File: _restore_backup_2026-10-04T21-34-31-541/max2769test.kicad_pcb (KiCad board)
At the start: 4 copper layers, 166 parts, among them J1 Conn_Coaxial, J2 RJ45_JK0654219, J3 Conn_01x03_Socket, J4 Conn_01x05_Pin, J5 USB_C_Receptacle_PowerOnly_6P, SW1 SW_Push, U1 MAX2769B, U10 TPS22918, U11 TPS22918, U12 BY25Q16AW, U2 ICE40UP5K-SG48ITR, U3 STM32C051K6T6, U4 TPS7A20, U5 TPS7A20, U6 TX22-M010S, U7 TPS7A20, U8 RTL8211FD, U9 TPS7A20, Y1 TSX-3225

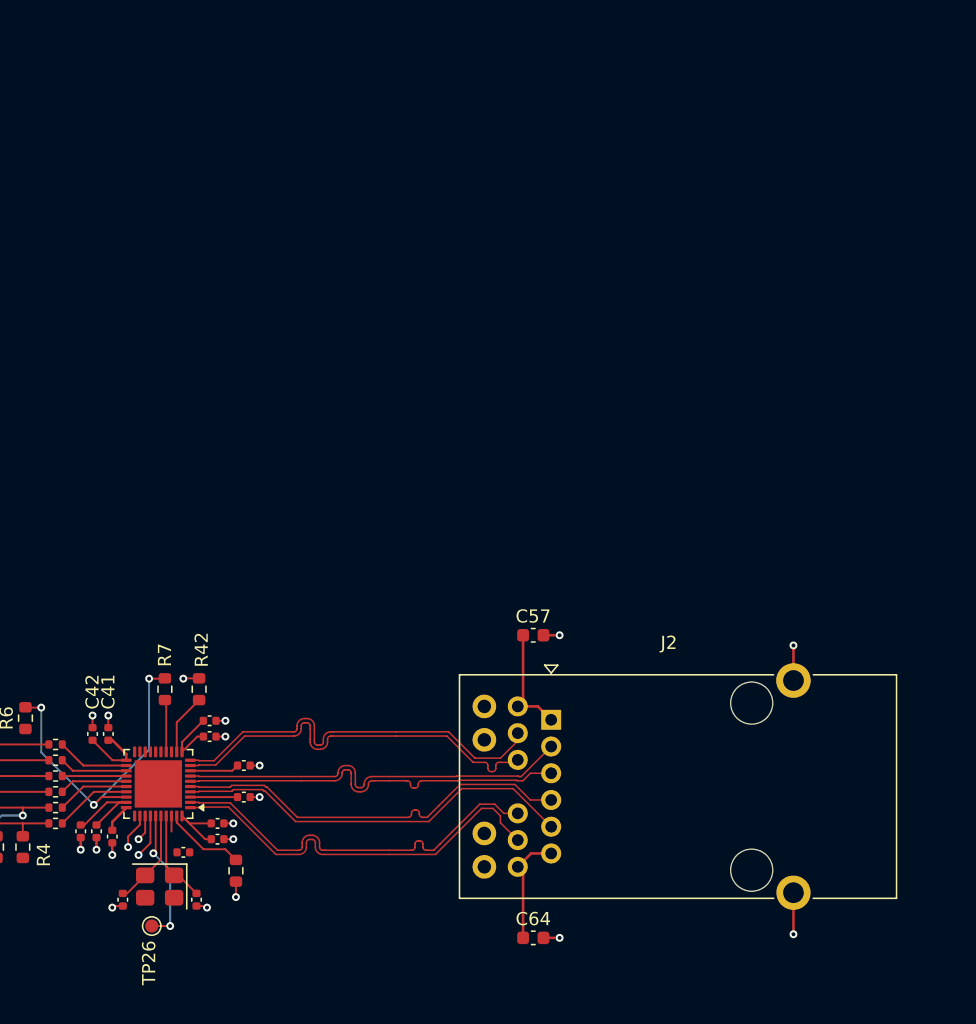
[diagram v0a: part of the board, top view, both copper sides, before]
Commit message: work on PHY layout
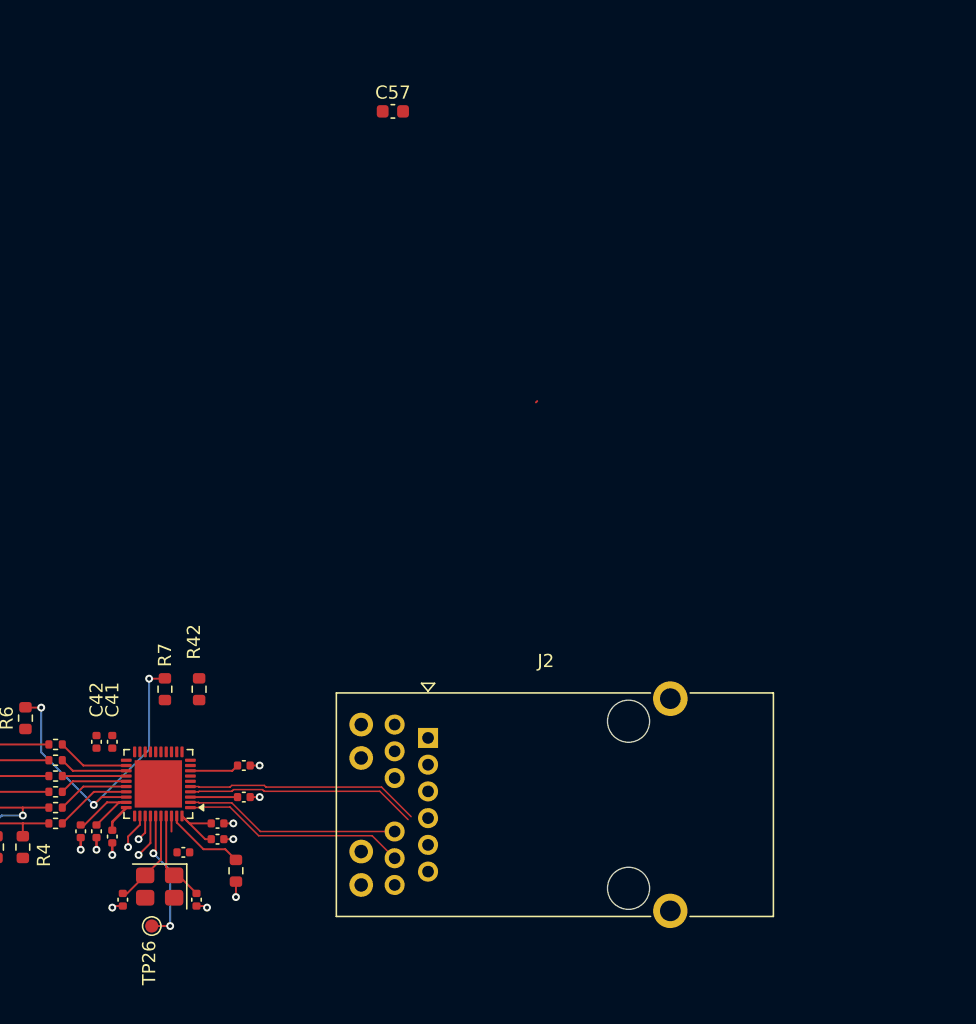
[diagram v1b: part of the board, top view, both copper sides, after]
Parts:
- removed C64: 100p, Capacitor_SMD:C_0603_1608Metric
- removed C65: 4.7u, Capacitor_SMD:C_0402_1005Metric
- removed C66: 100n, Capacitor_SMD:C_0402_1005Metric
- moved C57 41.2 mm to (194.3, 45.7)
- moved J2 9.46 mm to (197.0, 93.3)
- moved C41 0.67 mm to (173.0, 93.6)
- moved C42 0.67 mm to (171.8, 93.6)
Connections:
- C57 pad 1: Net-(J2-MXCT3) -> Net-(J2-MXCT1)
- J2 pad 1: Net-(J2-MXCT3) -> Net-(J2-MXCT1)
- J2 pad 4: /PHY_BI_DB_N -> /PHY_BI_DB_P
- J2 pad 5: /PHY_BI_DB_P -> /PHY_BI_DB_N
- J2 pad 7: Net-(J2-MXCT3) -> Net-(J2-MXCT1)
- J2 pad 8: /PHY_BI_DD_N -> /PHY_BI_DD_P
- J2 pad 9: /PHY_BI_DD_P -> /PHY_BI_DD_N
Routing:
- net /PHY_BI_DD_N: track 30.7 -> 0.00 mm
- net /PHY_BI_DC_N: track 30.6 -> 0.00 mm
- net /PHY_BI_DC_P: track 30.6 -> 0.00 mm
- net /PHY_BI_DD_P: track 30.6 -> 0.00 mm
- net /PHY_BI_DA_N: track 30.6 -> 16.4 mm
- net /PHY_BI_DA_P: track 30.7 -> 17.1 mm
- net /PHY_BI_DB_P: track 30.7 -> 17.6 mm
- net /PHY_BI_DB_N: track 30.7 -> 17.8 mm
- net GND: track 21.3 -> 8.51 mm, vias 19 -> 10
- net Net-(J2-MXCT3): track 8.54 -> 0.00 mm
- net Net-(J2-MXCT1): track 8.53 -> 0.00 mm
- net /PHY_LDO_OUT: track 16.1 -> 10.6 mm
- net /P3V3: track 17.7 -> 12.6 mm
- net /PHY_NRST: track 4.64 -> 0.00 mm
- net /PHY_MDIO: track 3.98 -> 0.00 mm
